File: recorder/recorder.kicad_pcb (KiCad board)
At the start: 4 copper layers, 605 x 15 mm, 34 parts, among them J1 GPIO_Conn_02x20_Odd_Even, U1 IM73D122V01, U10 TPS7A4700RGWT, U2 ADAU7118, U3 IM73D122V01, U4 IM73D122V01, U5 IM73D122V01, U6 IM73D122V01, U7 IM73D122V01, U8 IM73D122V01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

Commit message: v1
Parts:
- added R10: 2k2, Library:R_0603_1608Metric, F.Cu at (429.3, 295.5)
- added R11: 2k2, Library:R_0603_1608Metric, F.Cu at (429.3, 297.0)
- added R12: 22, Library:R_0603_1608Metric, F.Cu at (420.3, 307.5)
- added R13: 22, Library:R_0603_1608Metric, F.Cu at (431.8, 307.5)
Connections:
- U2 pad 1: /CLK0 -> Net-(U2-PDM_CLK0)
- U2 pad 4: /CLK1 -> Net-(U2-PDM_CLK1)
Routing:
- net /CLK1: track 542.0 -> 533.9 mm
- net Net-(U2-PDM_CLK0): track 0.00 -> 6.80 mm
- net Net-(U2-PDM_CLK1): track 0.00 -> 6.45 mm
- net /CLK0: track 543.4 -> 537.2 mm
- net /SCL: track 23.8 -> 29.4 mm, vias 1 -> 2
- net /IOVDD: track 78.0 -> 82.8 mm, vias 1 -> 3
- net /DAT0: track 371.9 -> 373.7 mm
- net /SDA: track 23.1 -> 24.6 mm, vias 1 -> 2
- net /DAT1: track 370.0 -> 371.2 mm
- net /DIN: track 15.3 -> 14.3 mm
- net /SCLK: track 47.8 -> 47.2 mm

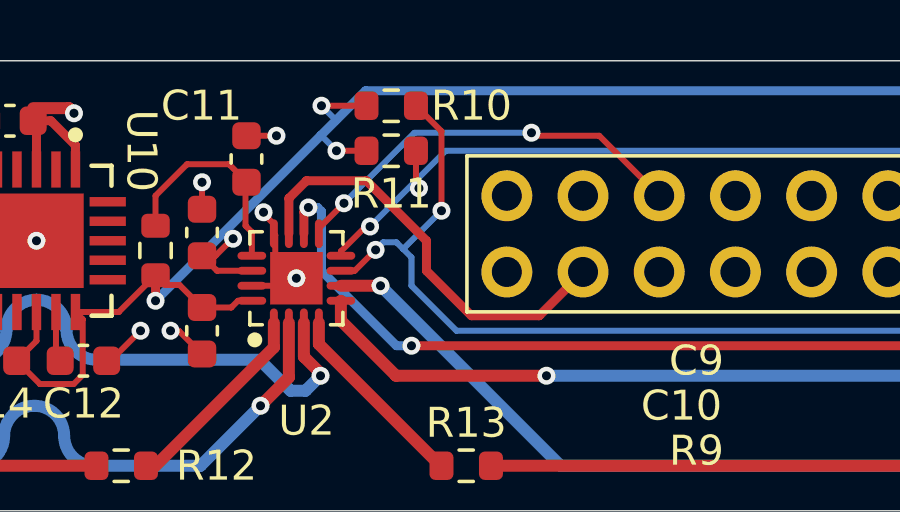
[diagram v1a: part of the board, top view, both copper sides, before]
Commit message: removed pull up resistors for SDA/SCL, they are on the jetson board
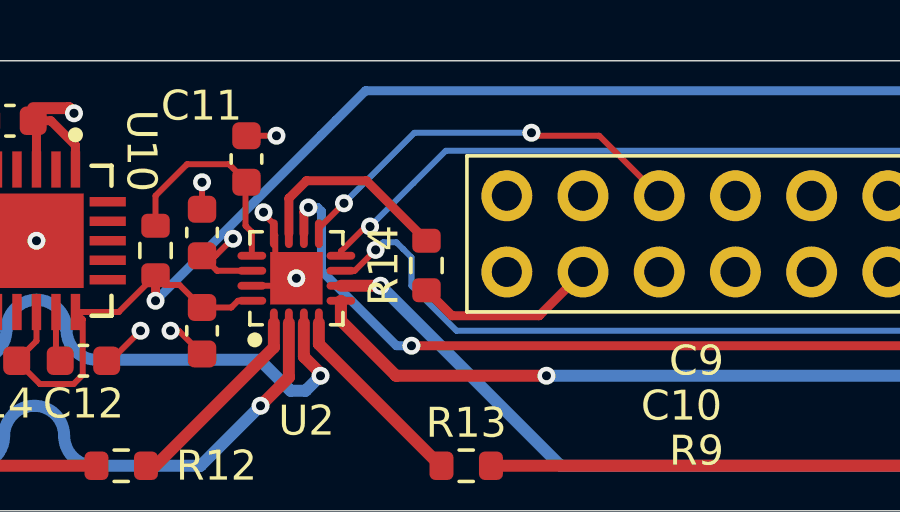
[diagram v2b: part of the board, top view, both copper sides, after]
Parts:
- removed R10, R11: 2k2, Library:R_0603_1608Metric
- added R14: 22, Library:R_0603_1608Metric, F.Cu at (430.5, 300.8)
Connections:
- U2 pad 11: /DIN -> Net-(U2-SDATA)
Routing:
- net /DIN: track 14.3 -> 6.18 mm
- net Net-(U2-SDATA): track 0.00 -> 6.84 mm
- net /SCL: track 29.4 -> 23.8 mm, vias 2 -> 1
- net /IOVDD: track 82.8 -> 78.8 mm, vias 3 -> 1
- net /SDA: track 24.6 -> 23.1 mm, vias 2 -> 1

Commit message: added drill holes
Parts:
- added REF**: MountingHole_2.1mm, MountingHole:MountingHole_2.1mm, F.Cu at (462.1, 305.5)
- added REF**: MountingHole_2.1mm, MountingHole:MountingHole_2.1mm, F.Cu at (435.9, 305.5)
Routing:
- net /DAT2: track 374.9 -> 377.0 mm

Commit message: increased width to 20mm, added mounting holes for waveshare case
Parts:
- added REF**: MountingHole_2.2mm_M2_ISO14580, Library:MountingHole_2.2mm_M2_ISO14580, F.Cu at (480.5, 311.0)
- added REF**: MountingHole_2.2mm_M2_ISO14580, Library:MountingHole_2.2mm_M2_ISO14580, F.Cu at (417.5, 311.0)
- REF** (x2): value MountingHole_2.1mm -> MountingHole_2.2mm_M2_ISO14580; footprint MountingHole:MountingHole_2.1mm -> Library:MountingHole_2.2mm_M2_ISO14580
- moved R13 1.50 mm to (431.8, 309.0)
- moved REF** 1.00 mm to (462.1, 306.5)
- moved REF** 1.00 mm to (435.9, 306.5)
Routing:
- net /DAT3: track 376.1 -> 379.2 mm
- net Net-(U2-PDM_CLK1): track 6.45 -> 7.96 mm
- net /DAT2: track 377.0 -> 375.7 mm
- net /CLK1: track 533.9 -> 534.9 mm
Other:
- board size 605 x 15 mm -> 605 x 20 mm

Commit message: Rounded corners, watermark
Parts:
- moved C1 1.00 mm to (151.3, 298.0)
- moved C10 1.00 mm to (423.0, 304.0)
- moved C11 1.00 mm to (424.5, 298.3)
- moved C12 1.00 mm to (419.1, 305.0)
- moved C13 1.00 mm to (416.6, 297.0)
- moved C14 1.00 mm to (416.1, 305.0)
- moved C2 1.00 mm to (236.3, 298.0)
- moved C3 1.00 mm to (321.3, 298.0)
- moved C4 1.00 mm to (406.3, 298.0)
- moved C5 1.00 mm to (491.2, 298.0)
- moved C6 1.00 mm to (576.2, 298.0)
- moved C7 1.00 mm to (661.2, 298.0)
- moved C8 1.00 mm to (746.2, 298.0)
- moved C9 1.00 mm to (423.0, 300.7)
- moved J1 1.00 mm to (481.4, 299.5)
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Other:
- outline, holes or cut-outs redrawn
- board text added: "HOFMEISTER ROBOTICS"
